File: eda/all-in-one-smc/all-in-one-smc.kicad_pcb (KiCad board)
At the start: 4 copper layers, 174.2 x 82.7 mm, 149 parts, among them J1 Audio out, J10 PS2, J11 SD-Card module, J2 PWR, J3 $1-3 latch, J4 ResetSwitch, J5 RomHighSel, J6 Expansion, J7 ProgrammingConnector, J8 VGA, J9 VIA Breakout, P1 USB_C_Plug_USB2.0, Q1 2N7002, Q2 2N7002, Q3 2N7002, Q4 2N7002, Q5 2N7002, SW1 BOOT, SW2 RST, U1 W65C02SxP, U10 74LHCT157, U11 28C256, U12 AS6C4008-55PCN, U13 74HCT138, U14 W65C51NxQ, U15 CH340K, U16 W25Q128JVS, U18 W65C22SxP, U19 RP2040, U2 4072, U20 W65C22SxP, U21 SN74LVC245APW, U22 SN74LVC245APW, U23 74HCT14, U24 74HCT86, U26 74HCT595, U27 74HCT165, U28 74AHCT541, U29 74HCT595, U3 74HCT32, U30 74HCT595, U31 74HCT138, U32 LM317L, U4 ATF16V8Bxx-xxPU, U5 74HCT139, U6 74HCT00, U7 NA555P, U8 74HCT273, U9 74LHCT157, X1 4Mhz, Y1 1.8432Mhz, Y2 ABM8-272-T3

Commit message: wip
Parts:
- removed JP1: IRQ Select, Connector_PinHeader_2.54mm:PinHeader_1x03_P2.54mm_Vertical
- removed JP3, JP4, JP5: ~, Connector_PinHeader_2.54mm:PinHeader_1x03_P2.54mm_Vertical
- removed P1: USB_C_Plug_USB2.0, Connector_USB:USB_C_Receptacle_GCT_USB4105-xx-A_16P_TopMnt_Horizontal
- removed R19, R22: 1k, Resistor_SMD:R_0805_2012Metric
- removed R20, R23: 2k, Resistor_SMD:R_0805_2012Metric
- removed R21, R24: 500, Resistor_SMD:R_0805_2012Metric
- removed U28: 74AHCT541, Package_SO:SOIC-20W_7.5x12.8mm_P1.27mm
- added BT1: CR2032, Battery:Battery_Panasonic_CR2032-HFN_Horizontal_CircularHoles, F.Cu at (143.8, 96.8)
- added C46: 6pf, Capacitor_SMD:C_0805_2012Metric, F.Cu at (135.4, 113.5)
- added C47: 6pf, Capacitor_SMD:C_0805_2012Metric, F.Cu at (137.8, 113.5)
- added J13: CS_Invert_Selection, Connector_PinHeader_2.54mm:PinHeader_2x03_P2.54mm_Horizontal, F.Cu at (260.4, 41.6)
- added J14: HDMI_A, Connector_Video:HDMI_A_Molex_208658-1001_Horizontal, F.Cu at (164.0, 41.8)
- added J15: USB_C Serial, Connector_USB:USB_C_Receptacle_GCT_USB4105-xx-A_16P_TopMnt_Horizontal, F.Cu at (180.6, 38.4)
- added R40: 10k, Resistor_SMD:R_0805_2012Metric, F.Cu at (260.4, 45.3)
- added R41: 10k, Resistor_SMD:R_0805_2012Metric, F.Cu at (263.0, 45.3)
- added R42: 10k, Resistor_SMD:R_0805_2012Metric, F.Cu at (265.5, 45.3)
- added R43: 2k2, Resistor_SMD:R_0805_2012Metric, F.Cu at (170.2, 52.8)
- added RN1: 270, Resistor_SMD:R_Array_Convex_8x0602, F.Cu at (162.3, 48.9)
- added U100: DS1306, Package_SO:TSSOP-20_4.4x5mm_P0.4mm, F.Cu at (142.9, 108.4)
- added Y3: 32.768kHz, Crystal:Crystal_C26-LF_D2.1mm_L6.5mm_Vertical, F.Cu at (137.4, 110.0)
- J2: value PWR -> PWR_Switch; footprint Connector_BarrelJack:BarrelJack_Horizontal -> Connector_PinHeader_2.54mm:PinHeader_1x02_P2.54mm_Vertical
- J8: value VGA -> USB_C PWR; footprint Connector_Dsub:DSUB-15-HD_Pins_Horizontal_P2.29x1.90mm_EdgePinOffset3.03mm_Housed_MountingHolesOffset4.94mm -> Connector_USB:USB_C_Receptacle_GCT_USB4105-xx-A_16P_TopMnt_Horizontal
- R16: value 47 -> 270
- R17: value 47 -> 5.1k
- R18: value 500 -> 5.1k
- R25: value 1k -> 2k2
- R26: value 2k -> 2k2
- moved C42 367.9 mm to (220.1, 70.6), turned to 90 degrees
- moved U27 365.6 mm to (213.6, 66.4), turned to -90 degrees
- moved J10 357.4 mm to (197.6, 39.1)
- moved C23 357.3 mm to (245.6, 66.2)
- moved C36 357.3 mm to (207.3, 56.7)
- moved C37 357.3 mm to (207.0, 48.4)
- moved C39 357.3 mm to (199.0, 53.8)
- moved D3 357.3 mm to (199.0, 51.4)
- moved J9 357.3 mm to (208.0, 41.6)
- moved JP2 357.3 mm to (194.8, 54.0)
- moved R28 357.3 mm to (191.5, 52.7)
- moved R29 357.3 mm to (202.7, 53.9)
- moved U18 357.3 mm to (249.3, 54.8)
- moved U20 357.3 mm to (230.2, 54.7)
- moved U29 357.3 mm to (213.6, 58.6)
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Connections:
- J1 pad 1: GND -> unconnected-(J1-Pin_1-Pad1)
- J1 pad 2: Audio_L -> unconnected-(J1-Pin_2-Pad2)
- J1 pad 3: Audio_R -> unconnected-(J1-Pin_3-Pad3)
- J2 pad 1: VCC -> Net-(J2-Pin_1)
- J2 pad 2: GND -> VCC
- J6 pad 45: GND -> Audio_R
- J6 pad 47: Audio_R -> Audio_GND
- J9 pad 24: unconnected-(J9-Pin_24-Pad24) -> GND
- J9 pad 26: unconnected-(J9-Pin_26-Pad26) -> /Expansion/~{IRQ}
- J9 pad 28: unconnected-(J9-Pin_28-Pad28) -> /IO/~{UserViaIRQ}
- J9 pad 30: unconnected-(J9-Pin_30-Pad30) -> /IO/~{NMI}
- R16 pad 1: Net-(U19-GPIO15) -> /GPU/DVI_CEC
- R16 pad 2: /GPU/VGA_Hsync -> Net-(J14-CEC)
- R17 pad 1: Net-(U19-GPIO16) -> Net-(J8-CC2)
- R17 pad 2: /GPU/VGA_VSync -> GND
- R18 pad 1: Net-(U19-GPIO17) -> Net-(J8-CC1)
- R18 pad 2: /GPU/VGA_R -> GND
- R25 pad 1: Net-(U19-GPIO24) -> /GPU/DVI_CEC
- R25 pad 2: /GPU/VGA_B -> +3.3V
- R26 pad 1: Net-(U19-GPIO25) -> /GPU/DVI_SCL
- R26 pad 2: /GPU/VGA_B -> VCC
- U18 pad 21: Net-(JP1-C) -> /IO/~{UserViaIRQ}
- U19 pad 18: Net-(U19-GPIO15) -> /GPU/DVI_CK-
- U19 pad 27: Net-(U19-GPIO16) -> /GPU/DVI_CK+
- U19 pad 28: Net-(U19-GPIO17) -> /GPU/DVI_D0-
- U19 pad 29: Net-(U19-GPIO18) -> /GPU/DVI_D0+
- U19 pad 30: Net-(U19-GPIO19) -> /GPU/DVI_D1-
- U19 pad 31: Net-(U19-GPIO20) -> /GPU/DVI_D1+
- U19 pad 32: Net-(U19-GPIO21) -> /GPU/DVI_D2-
- U19 pad 34: Net-(U19-GPIO22) -> /GPU/DVI_D2+
- U19 pad 35: Net-(U19-GPIO23) -> /GPU/DVI_SDA
- U19 pad 36: Net-(U19-GPIO24) -> /GPU/DVI_SCL
- U19 pad 37: Net-(U19-GPIO25) -> /GPU/DVI_CEC
- U27 pad 11: Net-(U27-D0) -> /IO/PS2 keyboard interface/DIO7
- U27 pad 12: Net-(U27-D1) -> /IO/PS2 keyboard interface/DIO6
- U27 pad 13: Net-(U27-D2) -> /IO/PS2 keyboard interface/DIO5
- U27 pad 14: Net-(U27-D3) -> /IO/PS2 keyboard interface/DIO4
- U27 pad 3: Net-(U27-D4) -> /IO/PS2 keyboard interface/DIO3
- U27 pad 4: Net-(U27-D5) -> /IO/PS2 keyboard interface/DIO2
- U27 pad 5: Net-(U27-D6) -> /IO/PS2 keyboard interface/DIO1
- U27 pad 6: Net-(U27-D7) -> /IO/PS2 keyboard interface/DIO0
- U6 pad 4: GND -> /IO/~{SPI_CS2}
- U6 pad 5: GND -> /IO/~{SPI_CS2}
- U6 pad 6: unconnected-(U6-Pad6) -> /IO/Clock/CS
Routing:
- net /D0: track 19.6 -> 228.1 mm, vias 0 -> 10
- net /D3: track 19.6 -> 215.8 mm, vias 0 -> 11
- net /D1: track 19.6 -> 211.6 mm, vias 0 -> 9
- net /D2: track 19.6 -> 208.7 mm, vias 0 -> 9
- net /Expansion/IoSelect1: track 0.00 -> 182.3 mm, vias 0 -> 4
- net /D4: track 19.6 -> 194.5 mm, vias 0 -> 9
- net Audio_R: track 0.00 -> 172.4 mm
- net Audio_GND: track 0.00 -> 171.0 mm
- net Audio_L: track 0.00 -> 169.4 mm
- net /D6: track 0.00 -> 169.3 mm, vias 0 -> 9
- net /D5: track 0.00 -> 167.7 mm, vias 0 -> 9
- net /D7: track 0.00 -> 165.9 mm, vias 0 -> 10
- net +3.3V: track 15.8 -> 178.5 mm, vias 0 -> 14
- net /A12: track 0.00 -> 137.9 mm, vias 0 -> 4
- net /IO/SPI_CLK: track 0.00 -> 134.6 mm, vias 0 -> 4
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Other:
- board size 174.2 x 82.7 mm -> 161.1 x 82.9 mm
- board text added: "PWR"
- board text added: "SERIAL"

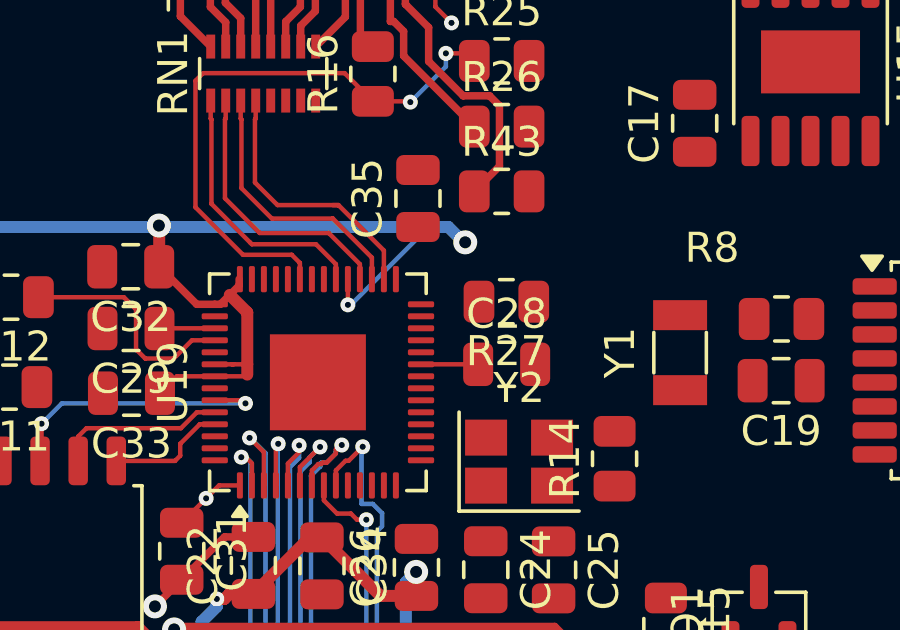
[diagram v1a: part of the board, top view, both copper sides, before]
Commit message: Incorrect mode on SD card
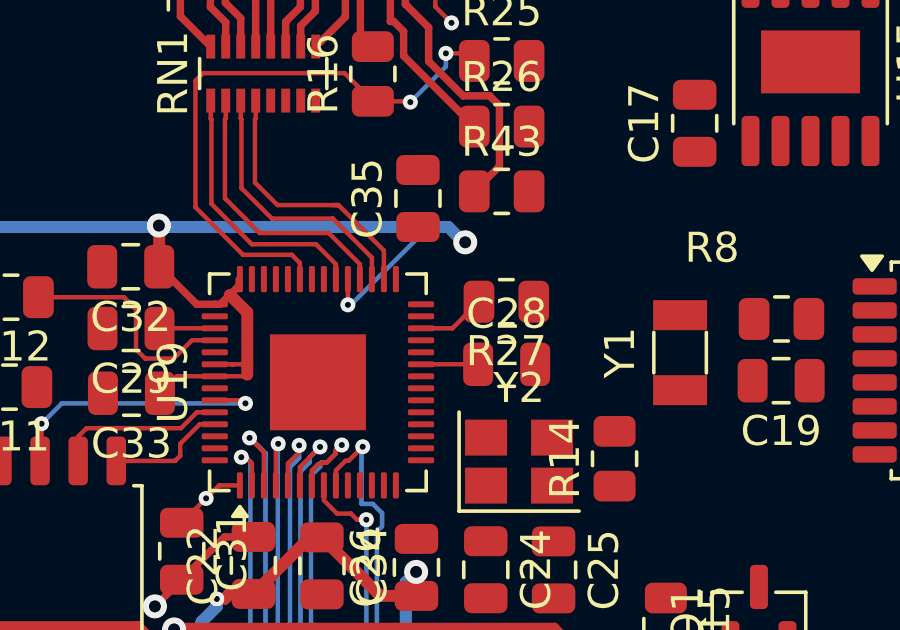
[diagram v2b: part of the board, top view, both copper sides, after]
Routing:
- net /GPU/RUN: track 4.10 -> 6.40 mm
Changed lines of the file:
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@@
+	)
+	(segment
+		(start 168.5843 57.3741)
+		(end 169.4707 56.4877)
+		(width 0.1524)
+		(layer "F.Cu")
+		(net 233)
+	)
+	(segment
+		(start 167.5384 57.3741)
+		(end 168.5843 57.3741)
+		(width 0.1524)
+		(layer "F.Cu")
+		(net 233)
 	)
 	(segment
